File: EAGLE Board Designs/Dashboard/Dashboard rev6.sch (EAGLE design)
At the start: 80 parts, among them J1 JUMPER__1X02, J2 CONNECTOR-8_μF_S_RA_, J3 CONNECTOR-CAN_μF_S_RA_, J4 CONNECTOR-6_μF_S_RA_, J6 CONNECTOR-6_μF_S_RA_, U10 NEOPIXEL, U11 NEOPIXEL, U12 NEOPIXEL, U13 NEOPIXEL, U14 NEOPIXEL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

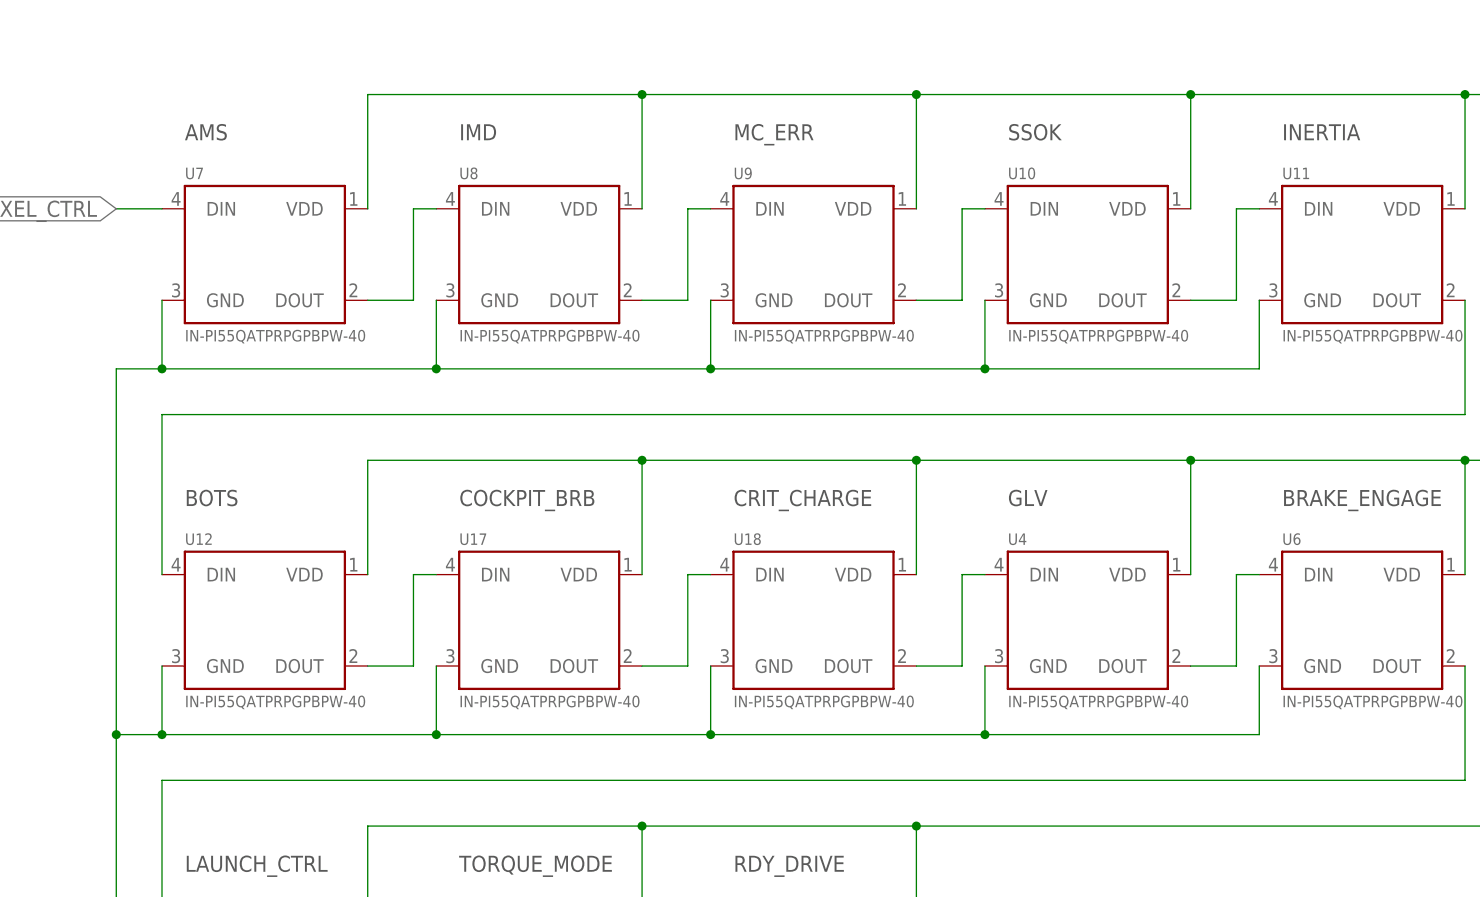
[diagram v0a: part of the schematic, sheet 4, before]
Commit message: Began placement
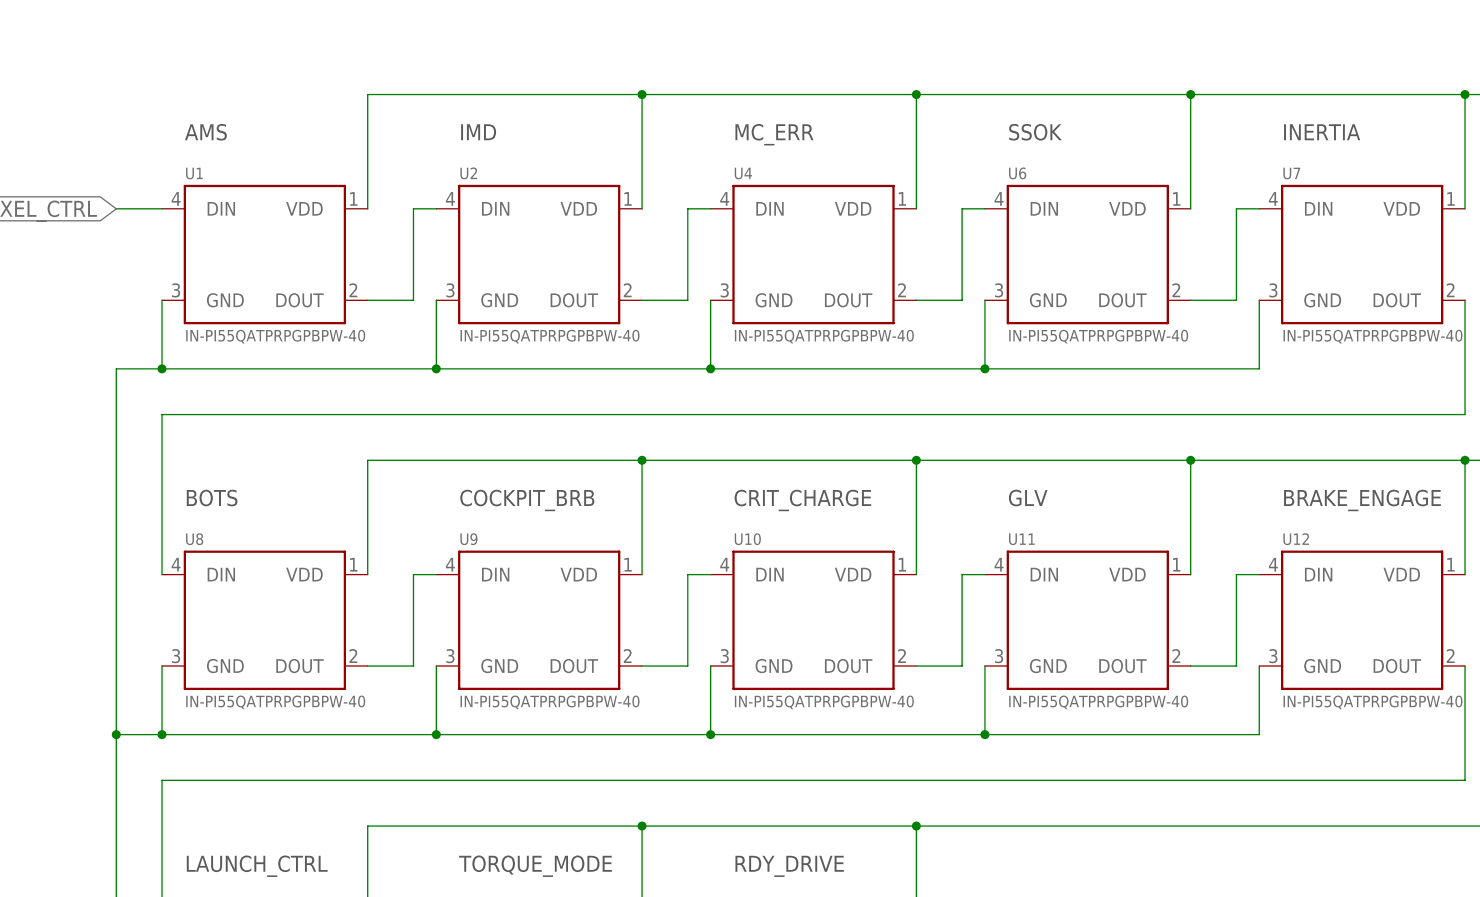
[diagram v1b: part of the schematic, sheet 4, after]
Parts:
- removed U17, U18: NEOPIXEL, HyTechDevices:NEOPIXEL
- added U1, U2: NEOPIXEL, HyTechDevices:NEOPIXEL
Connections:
- removed net N$11: U18.DOUT, U4.DIN
- removed net N$23 (its old number): U17.DOUT, U18.DIN
- removed net N$4 (its old number): U12.DOUT, U17.DIN
- new net N$5: U1.DOUT, U2.DIN
- new net N$6: U2.DOUT, U4.DIN
- new net N$8: U6.DOUT, U7.DIN
- net +5V: now also U1.VDD, U2.VDD; no longer U17.VDD, U18.VDD
- net GND: now also U1.GND, U2.GND; no longer U17.GND, U18.GND
- net N$27: now also U12.DOUT; no longer U6.DOUT
- net NEOPIXEL_CTRL: now also U1.DIN; no longer U7.DIN
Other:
- moved on the sheet: U10, U11, U12, U4, U6, U7, U8, U9

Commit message: More placements
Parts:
- removed XF2: FUSE_HOLDER_MINIBLADEPTH, HyTechDevices:FUSE_HOLDER_MINIBLADEPTH
- added XF1: FUSE_HOLDER_MINIBLADESMD, HyTechDevices:FUSE_HOLDER_MINIBLADESMD
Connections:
- net +24V: now also XF1.2; no longer XF2.2
- net 24VIN: now also XF1.1; no longer XF2.1
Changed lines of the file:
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@@
 <part name="R1" library="HyTechDevices" deviceset="RESISTOR_?_*" device="0603" technology="1K"/>
 <part name="R2" library="HyTechDevices" deviceset="RESISTOR_?_*" device="0603" technology="1K"/>
-<part name="XF2" library="HyTechDevices" deviceset="FUSE_HOLDER_*" device="PTH" technology="MINIBLADE"/>
 <part name="A4" library="HyTechDevices" deviceset="VOLTAGE_REGULATOR_MODULE_?_*" device="OKI-78SR" technology="12V"/>
 <part name="TP1_24V" library="HyTechDevices" deviceset="TEST_POINT" device=""/>
@@
 <part name="U14" library="HyTechDevices" deviceset="NEOPIXEL" device=""/>
 <part name="U15" library="HyTechDevices" deviceset="NEOPIXEL" device=""/>
+<part name="XF1" library="HyTechDevices" deviceset="FUSE_HOLDER_*" device="SMD" technology="MINIBLADE"/>
 </parts>
 <sheets>
@@
 <attribute name="RESISTANCE" x="222.25" y="146.05" size="1.27" layer="96" rot="R90" align="top-center"/>
 </instance>
-<instance part="XF2" gate="G$1" x="121.92" y="162.56" smashed="yes">
-<attribute name="NAME" x="121.92" y="163.322" size="1.27" layer="95" align="bottom-center"/>
-<attribute name="MPN" x="121.92" y="156.718" size="1.27" layer="96" align="top-center"/>
-</instance>
 <instance part="A4" gate="G$1" x="101.6" y="127" smashed="yes">
 <attribute name="NAME" x="101.6" y="127.762" size="1.27" layer="95"/>
@@
 <instance part="U$4" gate="G$1" x="93.98" y="127" smashed="yes">
 <attribute name="VALUE" x="93.98" y="132.08" size="1.778" layer="96" align="bottom-center"/>
+</instance>
+<instance part="XF1" gate="G$1" x="121.92" y="162.56" smashed="yes">
+<attribute name="NAME" x="121.92" y="163.322" size="1.27" layer="95" align="bottom-center"/>
+<attribute name="MPN" x="121.92" y="156.718" size="1.27" layer="96" align="top-center"/>
 </instance>
 </instances>
@@
 <wire x1="111.76" y1="154.94" x2="111.76" y2="160.02" width="0.1524" layer="91"/>
 <wire x1="111.76" y1="160.02" x2="114.3" y2="160.02" width="0.1524" layer="91"/>
-<pinref part="XF2" gate="G$1" pin="1"/>
 <pinref part="D6" gate="G$1" pin="C"/>
 <wire x1="111.76" y1="160.02" x2="106.68" y2="160.02" width="0.1524" layer="91"/>
 <junction x="111.76" y="160.02"/>
 <label x="106.68" y="160.02" size="1.27" layer="95" rot="R180" xref="yes"/>
+<pinref part="XF1" gate="G$1" pin="1"/>
 </segment>
 <segment>
@@
 </segment>
 <segment>
-<pinref part="XF2" gate="G$1" pin="2"/>
 <wire x1="132.08" y1="162.56" x2="132.08" y2="160.02" width="0.1524" layer="91"/>
 <wire x1="132.08" y1="160.02" x2="129.54" y2="160.02" width="0.1524" layer="91"/>
 <pinref part="U$1" gate="G$1" pin="+24V"/>
-</segment>
-<segment>
+<pinref part="XF1" gate="G$1" pin="2"/>
+</segment>
+<segment>

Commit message: Approx placements done
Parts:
- removed J1: JUMPER__1X02, HyTechDevices:JUMPER__1X02
- removed RN3: RESISTOR_NETWORK_4_1K, HyTechDevices:RESISTOR_NETWORK_4_1K
- added JP1: JUMPER_0603_, HyTechDevices:JUMPER_0603_
- added R6: RESISTOR_0603_1K, HyTechDevices:RESISTOR_0603_1K
- TP_24V: SIGNAL (none) -> +12V
- TP_BRB: SIGNAL (none) -> SHUTDOWN_H
- renumbered TP1_24V to TP_24V
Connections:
- net N$13 renamed A
- net N$14 renamed B
- net N$15 renamed C
- net N$17 renamed F
- net N$19 renamed D
- net N$2 renamed TEENSY_ON
- net N$25 renamed CRX
- net N$28 renamed HORNS
- net N$29 renamed CTX
- net N$39 renamed HORNB
- net N$50 renamed FEED
- removed net N$16: D101.G, RN4C.2
- removed net N$18: D101.E, RN4A.2
- removed net N$24: J1.2, R36.2
- new net E: D101.E, RN4C.2
- new net G: D101.G, RN4A.2
- new net N$10: JP1.2, R36.2
- net CANH: now also JP1.1; no longer J1.1
- net E2: now also RN4C.1; no longer RN4A.1
- net G2: now also RN4A.1; no longer RN4C.1
- net GND: now also R6.1; no longer RN3C.1
- net N$3: now also R6.2; no longer RN3C.2
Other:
- moved on the sheet: RN4A, RN4C

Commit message: Continued routing
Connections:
- net A: now also RN2D.2; no longer RN2A.2
- net A2: now also RN2D.1; no longer RN2A.1
- net B: now also RN2C.2; no longer RN2B.2
- net B2: now also RN2C.1; no longer RN2B.1
- net C: now also RN2B.2; no longer RN2C.2
- net C2: now also RN2B.1; no longer RN2C.1
- net D: now also RN2A.2; no longer RN2D.2
- net D2: now also RN2A.1; no longer RN2D.1
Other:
- moved on the sheet: RN2A, RN2B, RN2C, RN2D
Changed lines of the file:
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@@
 <attribute name="VALUE" x="190.5" y="179.07" size="1.27" layer="96" align="top-center"/>
 </instance>
-<instance part="RN2" gate="A" x="210.82" y="172.72" smashed="yes">
+<instance part="RN2" gate="A" x="205.74" y="165.1" smashed="yes">
+<attribute name="NAME" x="204.47" y="166.37" size="1.27" layer="95" align="bottom-center"/>
+<attribute name="RESISTANCE" x="204.47" y="163.83" size="1.27" layer="96" align="top-center"/>
+</instance>
+<instance part="RN2" gate="B" x="210.82" y="167.64" smashed="yes">
+<attribute name="NAME" x="209.55" y="168.91" size="1.27" layer="95" align="bottom-center"/>
+<attribute name="RESISTANCE" x="209.55" y="166.37" size="1.27" layer="96" align="top-center"/>
+</instance>
+<instance part="RN2" gate="C" x="205.74" y="170.18" smashed="yes">
+<attribute name="NAME" x="204.47" y="171.45" size="1.27" layer="95" align="bottom-center"/>
+<attribute name="RESISTANCE" x="204.47" y="168.91" size="1.27" layer="96" align="top-center"/>
+</instance>
+<instance part="RN2" gate="D" x="210.82" y="172.72" smashed="yes">
 <attribute name="NAME" x="209.55" y="173.99" size="1.27" layer="95" align="bottom-center"/>
 <attribute name="RESISTANCE" x="209.55" y="171.45" size="1.27" layer="96" align="top-center"/>
-</instance>
-<instance part="RN2" gate="B" x="205.74" y="170.18" smashed="yes">
-<attribute name="NAME" x="204.47" y="171.45" size="1.27" layer="95" align="bottom-center"/>
-<attribute name="RESISTANCE" x="204.47" y="168.91" size="1.27" layer="96" align="top-center"/>
-</instance>
-<instance part="RN2" gate="C" x="210.82" y="167.64" smashed="yes">
-<attribute name="NAME" x="209.55" y="168.91" size="1.27" layer="95" align="bottom-center"/>
-<attribute name="RESISTANCE" x="209.55" y="166.37" size="1.27" layer="96" align="top-center"/>
-</instance>
-<instance part="RN2" gate="D" x="205.74" y="165.1" smashed="yes">
-<attribute name="NAME" x="204.47" y="166.37" size="1.27" layer="95" align="bottom-center"/>
-<attribute name="RESISTANCE" x="204.47" y="163.83" size="1.27" layer="96" align="top-center"/>
 </instance>
 <instance part="RN4" gate="A" x="210.82" y="157.48" smashed="yes">
@@
 </segment>
 </net>
-<net name="A2" class="0">
-<segment>
-<wire x1="198.12" y1="172.72" x2="205.74" y2="172.72" width="0.1524" layer="91"/>
-<pinref part="RN2" gate="A" pin="1"/>
-<pinref part="U3" gate="G$1" pin="GPA0"/>
-</segment>
-</net>
-<net name="B2" class="0">
-<segment>
-<wire x1="198.12" y1="170.18" x2="200.66" y2="170.18" width="0.1524" layer="91"/>
-<pinref part="RN2" gate="B" pin="1"/>
-<pinref part="U3" gate="G$1" pin="GPA1"/>
-</segment>
-</net>
-<net name="C2" class="0">
-<segment>
-<wire x1="198.12" y1="167.64" x2="205.74" y2="167.64" width="0.1524" layer="91"/>
-<pinref part="RN2" gate="C" pin="1"/>
-<pinref part="U3" gate="G$1" pin="GPA2"/>
-</segment>
-</net>
-<net name="D2" class="0">
-<segment>
-<wire x1="198.12" y1="165.1" x2="200.66" y2="165.1" width="0.1524" layer="91"/>
-<pinref part="RN2" gate="D" pin="1"/>
-<pinref part="U3" gate="G$1" pin="GPA3"/>
-</segment>
-</net>
-<net name="A" class="0">
-<segment>
-<pinref part="D101" gate="G$1" pin="A"/>
-<wire x1="213.36" y1="172.72" x2="226.06" y2="172.72" width="0.1524" layer="91"/>
-<pinref part="RN2" gate="A" pin="2"/>
-</segment>
-</net>
 <net name="B" class="0">
 <segment>
-<wire x1="208.28" y1="170.18" x2="218.44" y2="170.18" width="0.1524" layer="91"/>
 <wire x1="218.44" y1="170.18" x2="218.44" y2="180.34" width="0.1524" layer="91"/>
 <wire x1="218.44" y1="180.34" x2="259.08" y2="180.34" width="0.1524" layer="91"/>
@@
 <pinref part="D101" gate="G$1" pin="B"/>
 <wire x1="259.08" y1="167.64" x2="256.54" y2="167.64" width="0.1524" layer="91"/>
-<pinref part="RN2" gate="B" pin="2"/>
+<pinref part="RN2" gate="C" pin="2"/>
+<wire x1="208.28" y1="170.18" x2="218.44" y2="170.18" width="0.1524" layer="91"/>
 </segment>
 </net>
 <net name="C" class="0">
 <segment>
-<wire x1="213.36" y1="167.64" x2="215.9" y2="167.64" width="0.1524" layer="91"/>
 <wire x1="215.9" y1="167.64" x2="215.9" y2="182.88" width="0.1524" layer="91"/>
 <wire x1="215.9" y1="182.88" x2="261.62" y2="182.88" width="0.1524" layer="91"/>
@@
 <wire x1="261.62" y1="182.88" x2="261.62" y2="152.4" width="0.1524" layer="91"/>
 <wire x1="261.62" y1="152.4" x2="256.54" y2="152.4" width="0.1524" layer="91"/>
-<pinref part="RN2" gate="C" pin="2"/>
+<pinref part="RN2" gate="B" pin="2"/>
+<wire x1="213.36" y1="167.64" x2="215.9" y2="167.64" width="0.1524" layer="91"/>
 </segment>
 </net>
@@
 <net name="D" class="0">
 <segment>
-<wire x1="208.28" y1="165.1" x2="215.9" y2="165.1" width="0.1524" layer="91"/>
 <pinref part="D101" gate="G$1" pin="D"/>
 <wire x1="215.9" y1="165.1" x2="215.9" y2="147.32" width="0.1524" layer="91"/>
 <wire x1="215.9" y1="147.32" x2="226.06" y2="147.32" width="0.1524" layer="91"/>
-<pinref part="RN2" gate="D" pin="2"/>
+<pinref part="RN2" gate="A" pin="2"/>
+<wire x1="208.28" y1="165.1" x2="215.9" y2="165.1" width="0.1524" layer="91"/>
 </segment>
 </net>
@@
 </segment>
 </net>
+<net name="A2" class="0">
+<segment>
+<pinref part="U3" gate="G$1" pin="GPA0"/>
+<pinref part="RN2" gate="D" pin="1"/>
+<wire x1="198.12" y1="172.72" x2="205.74" y2="172.72" width="0.1524" layer="91"/>
+</segment>
+</net>
+<net name="A" class="0">
+<segment>
+<pinref part="RN2" gate="D" pin="2"/>
+<pinref part="D101" gate="G$1" pin="A"/>
+<wire x1="213.36" y1="172.72" x2="226.06" y2="172.72" width="0.1524" layer="91"/>
+</segment>
+</net>
+<net name="B2" class="0">
+<segment>
+<pinref part="RN2" gate="C" pin="1"/>
+<pinref part="U3" gate="G$1" pin="GPA1"/>
+<wire x1="200.66" y1="170.18" x2="198.12" y2="170.18" width="0.1524" layer="91"/>
+</segment>
+</net>
+<net name="C2" class="0">
+<segment>
+<pinref part="U3" gate="G$1" pin="GPA2"/>
+<pinref part="RN2" gate="B" pin="1"/>
+<wire x1="198.12" y1="167.64" x2="205.74" y2="167.64" width="0.1524" layer="91"/>
+</segment>
+</net>
+<net name="D2" class="0">
+<segment>
+<pinref part="RN2" gate="A" pin="1"/>
+<pinref part="U3" gate="G$1" pin="GPA3"/>
+<wire x1="200.66" y1="165.1" x2="198.12" y2="165.1" width="0.1524" layer="91"/>
+</segment>
+</net>

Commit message: Validated design
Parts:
- removed D2: TVS_30VDO-214AA, HyTechDevices:TVS_30VDO-214AA
- removed R15: RESISTOR_0603_41.2K, HyTechDevices:RESISTOR_0603_41.2K
- removed R7: RESISTOR_0603_5.1K, HyTechDevices:RESISTOR_0603_5.1K
- removed TP_BOTS, TP_BRB, TP_INERTIA, TP_SSOK: TEST_POINT, HyTechDevices:TEST_POINT
- added TP2, TP3, TP4: TEST_POINT, HyTechDevices:TEST_POINT
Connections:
- removed net SSOK: D2.C, J2.7, R15.1, TP_SSOK.1
- removed net SSOK_READ: A2.A0, R15.2, R7.1
- net BOTS: now also TP3.1; no longer TP_BOTS.1
- net BRB: now also TP4.1; no longer TP_BRB.1
- net GND: no longer D2.A, R7.2
- net INERTIA: now also TP2.1; no longer TP_INERTIA.1
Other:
- note added: "GEN_PURP"
- note removed: "SSOK"

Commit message: updated from latest library
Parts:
- D3, D4, D5, D6: value TVS_30VDO-214AA -> TVS_DO-214AA_30V; device HyTechDevices:TVS_30VDO-214AA -> HyTechDevices:TVS_DO-214AA_30V
- U1, U10, U11, U12, U13, U14, U15, U2, U4, U6, U7, U8, U9: value NEOPIXEL -> NEOPIXEL_IN-PI55QATPRPGPBPW-40; device HyTechDevices:NEOPIXEL -> HyTechDevices:NEOPIXEL_IN-PI55QATPRPGPBPW-40
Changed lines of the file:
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@@
 <part name="24V" library="HyTechDevices" deviceset="LED_?_*" device="0603" technology="ORANGE"/>
 <part name="R83" library="HyTechDevices" deviceset="RESISTOR_?_*" device="0603" technology="3.3K"/>
-<part name="D6" library="HyTechDevices" deviceset="TVS_*" device="DO-214AA" technology="30V"/>
+<part name="D6" library="HyTechDevices" deviceset="TVS_?_*" device="DO-214AA" technology="30V"/>
 <part name="P16" library="HyTechSupplies" deviceset="GND" device=""/>
 <part name="P17" library="HyTechSupplies" deviceset="GND" device=""/>
@@
 <part name="R14" library="HyTechDevices" deviceset="RESISTOR_?_*" device="0603" technology="5.1K"/>
 <part name="P21" library="HyTechSupplies" deviceset="GND" device=""/>
-<part name="D3" library="HyTechDevices" deviceset="TVS_*" device="DO-214AA" technology="30V"/>
+<part name="D3" library="HyTechDevices" deviceset="TVS_?_*" device="DO-214AA" technology="30V"/>
 <part name="P22" library="HyTechSupplies" deviceset="GND" device=""/>
-<part name="D4" library="HyTechDevices" deviceset="TVS_*" device="DO-214AA" technology="30V"/>
+<part name="D4" library="HyTechDevices" deviceset="TVS_?_*" device="DO-214AA" technology="30V"/>
 <part name="P25" library="HyTechSupplies" deviceset="GND" device=""/>
-<part name="D5" library="HyTechDevices" deviceset="TVS_*" device="DO-214AA" technology="30V"/>
+<part name="D5" library="HyTechDevices" deviceset="TVS_?_*" device="DO-214AA" technology="30V"/>
 <part name="R3" library="HyTechDevices" deviceset="RESISTOR_?_*" device="0603" technology="41.2K"/>
 <part name="R4" library="HyTechDevices" deviceset="RESISTOR_?_*" device="0603" technology="41.2K"/>
@@
 <part name="U$3" library="HyTechSupplies" deviceset="+24V" device=""/>
 <part name="U$4" library="HyTechSupplies" deviceset="+24V" device=""/>
-<part name="U1" library="HyTechDevices" deviceset="NEOPIXEL" device=""/>
-<part name="U2" library="HyTechDevices" deviceset="NEOPIXEL" device=""/>
-<part name="U4" library="HyTechDevices" deviceset="NEOPIXEL" device=""/>
-<part name="U6" library="HyTechDevices" deviceset="NEOPIXEL" device=""/>
-<part name="U7" library="HyTechDevices" deviceset="NEOPIXEL" device=""/>
-<part name="U8" library="HyTechDevices" deviceset="NEOPIXEL" device=""/>
-<part name="U9" library="HyTechDevices" deviceset="NEOPIXEL" device=""/>
-<part name="U10" library="HyTechDevices" deviceset="NEOPIXEL" device=""/>
-<part name="U11" library="HyTechDevices" deviceset="NEOPIXEL" device=""/>
-<part name="U12" library="HyTechDevices" deviceset="NEOPIXEL" device=""/>
-<part name="U13" library="HyTechDevices" deviceset="NEOPIXEL" device=""/>
-<part name="U14" library="HyTechDevices" deviceset="NEOPIXEL" device=""/>
-<part name="U15" library="HyTechDevices" deviceset="NEOPIXEL" device=""/>
+<part name="U1" library="HyTechDevices" deviceset="NEOPIXEL_*" device="IN-PI55QATPRPGPBPW-40"/>
+<part name="U2" library="HyTechDevices" deviceset="NEOPIXEL_*" device="IN-PI55QATPRPGPBPW-40"/>
+<part name="U4" library="HyTechDevices" deviceset="NEOPIXEL_*" device="IN-PI55QATPRPGPBPW-40"/>
+<part name="U6" library="HyTechDevices" deviceset="NEOPIXEL_*" device="IN-PI55QATPRPGPBPW-40"/>
+<part name="U7" library="HyTechDevices" deviceset="NEOPIXEL_*" device="IN-PI55QATPRPGPBPW-40"/>
+<part name="U8" library="HyTechDevices" deviceset="NEOPIXEL_*" device="IN-PI55QATPRPGPBPW-40"/>
+<part name="U9" library="HyTechDevices" deviceset="NEOPIXEL_*" device="IN-PI55QATPRPGPBPW-40"/>
+<part name="U10" library="HyTechDevices" deviceset="NEOPIXEL_*" device="IN-PI55QATPRPGPBPW-40"/>
+<part name="U11" library="HyTechDevices" deviceset="NEOPIXEL_*" device="IN-PI55QATPRPGPBPW-40"/>
+<part name="U12" library="HyTechDevices" deviceset="NEOPIXEL_*" device="IN-PI55QATPRPGPBPW-40"/>
+<part name="U13" library="HyTechDevices" deviceset="NEOPIXEL_*" device="IN-PI55QATPRPGPBPW-40"/>
+<part name="U14" library="HyTechDevices" deviceset="NEOPIXEL_*" device="IN-PI55QATPRPGPBPW-40"/>
+<part name="U15" library="HyTechDevices" deviceset="NEOPIXEL_*" device="IN-PI55QATPRPGPBPW-40"/>
 <part name="XF1" library="HyTechDevices" deviceset="FUSE_HOLDER_*" device="SMD" technology="MINIBLADE"/>
 <part name="TP_24V" library="HyTechDevices" deviceset="TEST_POINT" device="">
